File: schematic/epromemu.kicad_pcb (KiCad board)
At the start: 2 copper layers, 80.5 x 53.6 mm, 10 parts, among them J1 EPROM Connector, U1 Teensy4.1, U2 74HC245, U3 74HC245, U4 74HC245, U5 74HC245

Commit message: tweaks
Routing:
- net GND: track 0.00 -> 106.6 mm
- net +3V3: track 0.00 -> 11.4 mm
- net +5V: track 0.00 -> 3.70 mm
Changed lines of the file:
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@@
     (effects (font (size 1 1) (thickness 0.15)))
   )
+  (segment (start 109.4196 113.3404) (end 111.3246 113.3404) (width 0.1524) (layer "F.Cu") (net 1))
+  (segment (start 111.3246 113.3404) (end 112.5946 112.0704) (width 0.1524) (layer "F.Cu") (net 1))
+  (segment (start 168.3946 118.3404) (end 169.7446 119.6904) (width 0.1524) (layer "F.Cu") (net 8))
+  (segment (start 109.2926 81.1294) (end 134.1046 81.1294) (width 0.1524) (layer "F.Cu") (net 8))
+  (segment (start 134.1046 81.1294) (end 135.4546 82.4794) (width 0.1524) (layer "F.Cu") (net 8))
+  (segment (start 143.5826 118.3404) (end 168.3946 118.3404) (width 0.1524) (layer "F.Cu") (net 8))
+  (segment (start 143.7096 81.1294) (end 168.3946 81.1294) (width 0.1524) (layer "F.Cu") (net 8))
+  (segment (start 168.3946 81.1294) (end 169.7446 82.4794) (width 0.1524) (layer "F.Cu") (net 8))
+  (segment (start 109.4196 118.3404) (end 134.1046 118.3404) (width 0.1524) (layer "F.Cu") (net 8))
+  (segment (start 134.1046 118.3404) (end 135.4546 119.6904) (width 0.1524) (layer "F.Cu") (net 8))
+  (segment (start 109.2926 76.1294) (end 111.3246 76.1294) (width 0.1524) (layer "F.Cu") (net 33))
+  (segment (start 111.3246 76.1294) (end 112.5946 74.8594) (width 0.1524) (layer "F.Cu") (net 33))
+  (segment (start 145.6146 113.3404) (end 146.8846 112.0704) (width 0.1524) (layer "F.Cu") (net 33))
+  (segment (start 143.7096 76.1294) (end 145.6146 76.1294) (width 0.1524) (layer "F.Cu") (net 33))
+  (segment (start 145.6146 76.1294) (end 146.8846 74.8594) (width 0.1524) (layer "F.Cu") (net 33))
+  (segment (start 143.5826 113.3404) (end 145.6146 113.3404) (width 0.1524) (layer "F.Cu") (net 33))
 )

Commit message: v2 updates
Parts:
- added C6: 0.1uf, Capacitor_THT:C_Disc_D5.0mm_W2.5mm_P5.00mm, F.Cu at (132.1, 94.7)
- added U6: 74LS32, Package_DIP:DIP-14_W7.62mm_Socket, F.Cu at (135.2, 101.0)
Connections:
- U1 pad 21: CE_OE -> unconnected-(U1-Pad21)
- U1 pad 22: OE_3V3 -> unconnected-(U1-Pad22)
- U1 pad 23: CE_3V3 -> unconnected-(U1-Pad23)
- U2 pad 19: CE_OE -> Net-(U2-Pad19)
- U3 pad 11: CE_3V3 -> unconnected-(U3-Pad11)
- U3 pad 12: OE_3V3 -> unconnected-(U3-Pad12)
- U3 pad 8: OE_5V -> unconnected-(U3-Pad8)
- U3 pad 9: CE_5V -> unconnected-(U3-Pad9)
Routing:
- net GND: track 106.6 -> 280.7 mm
- net +3V3: track 11.4 -> 156.7 mm
- net +5V: track 3.70 -> 110.4 mm
- net D5_5V: track 0.00 -> 96.8 mm
- net A8_5V: track 0.00 -> 96.6 mm
- net D4_5V: track 0.00 -> 96.3 mm
- net A6_5V: track 0.00 -> 95.3 mm
- net A9_5V: track 0.00 -> 92.5 mm
- net D2_5V: track 0.00 -> 89.7 mm
- net D0_5V: track 0.00 -> 87.1 mm
- net A7_5V: track 0.00 -> 84.4 mm
- net A11_5V: track 0.00 -> 82.4 mm
- net D3_5V: track 0.00 -> 81.8 mm
- net D1_5V: track 0.00 -> 73.9 mm, vias 0 -> 1
- net A10_5V: track 0.00 -> 66.1 mm, vias 0 -> 2
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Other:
- rule pad_to_mask_clearance: 0.0508 -> 0

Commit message: starting v0.3
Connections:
- J1 pad 1: +5V -> A19_5V
- U1 pad 2: unconnected-(U1-Pad2) -> A19_3V3
- U1 pad 20: A18_3V3 -> unconnected-(U1-Pad20)
- U1 pad 3: unconnected-(U1-Pad3) -> A18_3V3
- U1 pad 48: unconnected-(U1-Pad48) -> +5V
- U3 pad 13: unconnected-(U3-Pad13) -> A15_3V3
- U3 pad 14: A18_3V3 -> A14_3V3
- U3 pad 15: A15_3V3 -> A17_3V3
- U3 pad 16: A14_3V3 -> A16_3V3
- U3 pad 17: A17_3V3 -> A18_3V3
- U3 pad 18: A16_3V3 -> A19_3V3
- U3 pad 2: A16_5V -> A19_5V
- U3 pad 3: A17_5V -> A18_5V
- U3 pad 4: A14_5V -> A16_5V
- U3 pad 5: A15_5V -> A17_5V
- U3 pad 6: A18_5V -> A14_5V
- U3 pad 7: unconnected-(U3-Pad7) -> A15_5V
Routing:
- net GND: track 280.7 -> 0.00 mm
- net +3V3: track 156.7 -> 0.00 mm
- net +5V: track 110.4 -> 0.00 mm
- net D5_5V: track 96.8 -> 0.00 mm
- net A8_5V: track 96.6 -> 0.00 mm
- net D4_5V: track 96.3 -> 0.00 mm
- net A6_5V: track 95.3 -> 0.00 mm
- net A9_5V: track 92.5 -> 0.00 mm
- net D2_5V: track 89.7 -> 0.00 mm
- net D0_5V: track 87.1 -> 0.00 mm
- net A7_5V: track 84.4 -> 0.00 mm
- net A11_5V: track 82.4 -> 0.00 mm
- net D3_5V: track 81.8 -> 0.00 mm
- net D1_5V: track 73.9 -> 0.00 mm, vias 1 -> 0
- net A10_5V: track 66.1 -> 0.00 mm, vias 2 -> 0
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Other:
- board size 80.5 x 53.6 mm -> 81 x 53.6 mm
- board text added: "1"
- board text added: "EPROM Emulator v0.3 - Brian Peek"
- board text removed: "EPROM Emulator v0.2 - Brian Peek"

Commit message: a complete v3?
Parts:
- added JP1: PWR, Connector_PinHeader_2.54mm:PinHeader_1x02_P2.54mm_Vertical, F.Cu at (156.3, 95.9)
- U6: value 74LS32 -> 74HC32
- moved U6 6.09 mm to (129.2, 101.0)
- moved C6 6.09 mm to (126.0, 94.7)
- moved J1 2.24 mm to (183.2, 115.9)
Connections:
- J1 pad 32: +5V -> Net-(J1-Pin_32)
- U1 pad 16: A16_3V3 -> unconnected-(U1-24_A10_TX6_SCL2-Pad16)
- U1 pad 17: A17_3V3 -> unconnected-(U1-25_A11_RX6_SDA2-Pad17)
- U1 pad 2: A19_3V3 -> unconnected-(U1-0_RX1_CRX2_CS1-Pad2)
- U1 pad 25: unconnected-(U1-Pad25) -> A19_3V3
- U1 pad 3: A18_3V3 -> unconnected-(U1-1_TX1_CTX2_MISO1-Pad3)
- U1 pad 4: unconnected-(U1-Pad4) -> A16_3V3
- U1 pad 5: unconnected-(U1-Pad5) -> A17_3V3
- U1 pad 6: unconnected-(U1-Pad6) -> A18_3V3
- U3 pad 13: A15_3V3 -> unconnected-(U3-B5-Pad13)
- U3 pad 14: A14_3V3 -> A15_3V3
- U3 pad 15: A17_3V3 -> A14_3V3
- U3 pad 16: A16_3V3 -> A18_3V3
- U3 pad 17: A18_3V3 -> A17_3V3
- U3 pad 18: A19_3V3 -> A16_3V3
- U3 pad 2: A19_5V -> A16_5V
- U3 pad 3: A18_5V -> A17_5V
- U3 pad 4: A16_5V -> A18_5V
- U3 pad 5: A17_5V -> A14_5V
- U3 pad 6: A14_5V -> A15_5V
- U3 pad 7: A15_5V -> unconnected-(U3-A5-Pad7)
- U5 pad 12: unconnected-(U5-Pad12) -> A19_5V
- U5 pad 8: unconnected-(U5-Pad8) -> A19_3V3
- U6 pad 11: GND -> unconnected-(U6-Pad11)
- U6 pad 6: GND -> unconnected-(U6-Pad6)
- U6 pad 8: GND -> unconnected-(U6-Pad8)
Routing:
- net GND: track 0.00 -> 250.0 mm
- net D5_5V: track 0.00 -> 112.5 mm
- net D4_5V: track 0.00 -> 108.5 mm
- net D2_5V: track 0.00 -> 104.3 mm
- net D0_5V: track 0.00 -> 103.2 mm
- net +3V3: track 0.00 -> 99.4 mm
- net D6_5V: track 0.00 -> 86.6 mm
- net D7_5V: track 0.00 -> 80.5 mm
- net D1_5V: track 0.00 -> 79.0 mm, vias 0 -> 1
- net A8_5V: track 0.00 -> 78.4 mm
- net D3_5V: track 0.00 -> 77.7 mm, vias 0 -> 1
- net A9_5V: track 0.00 -> 76.6 mm
- net CE_5V: track 0.00 -> 72.7 mm, vias 0 -> 1
- net +5V: track 0.00 -> 71.7 mm
- net A11_5V: track 0.00 -> 70.5 mm
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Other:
- board size 81 x 53.6 mm -> 82 x 53.7 mm

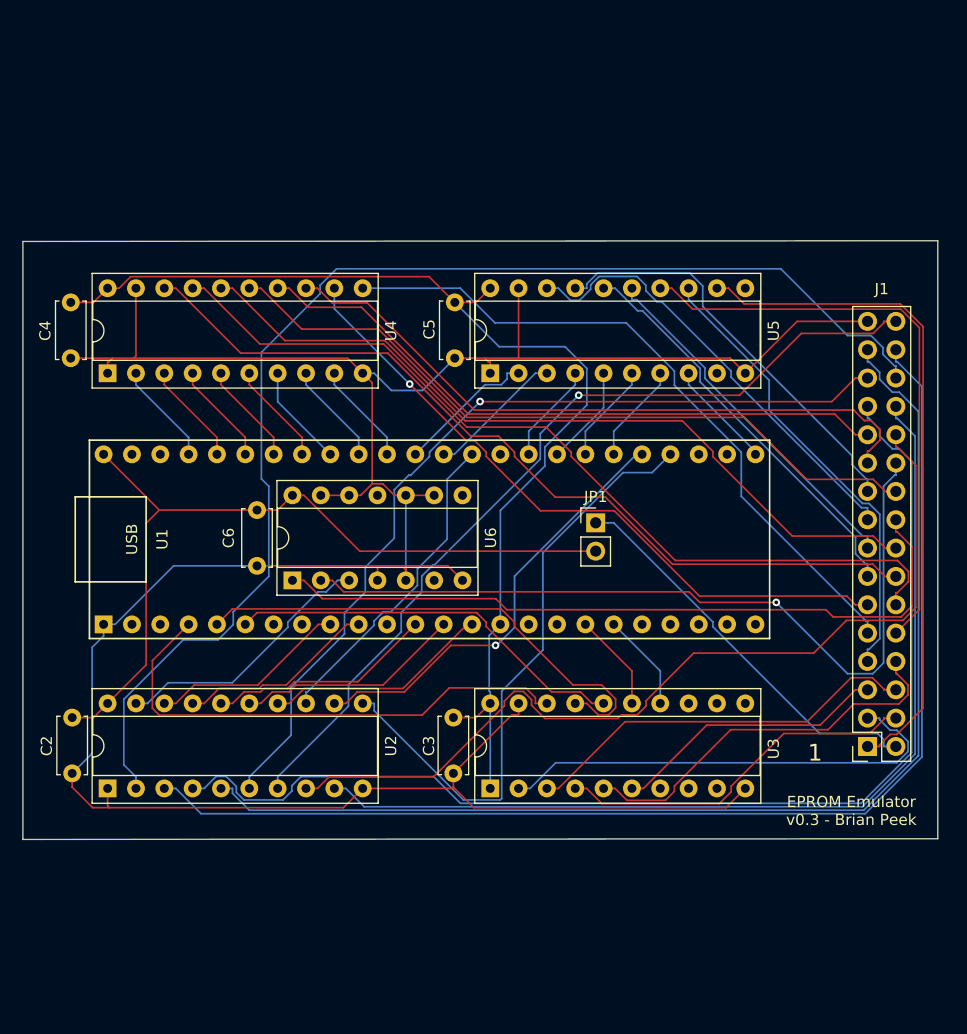
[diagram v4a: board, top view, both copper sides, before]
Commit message: mounting holes
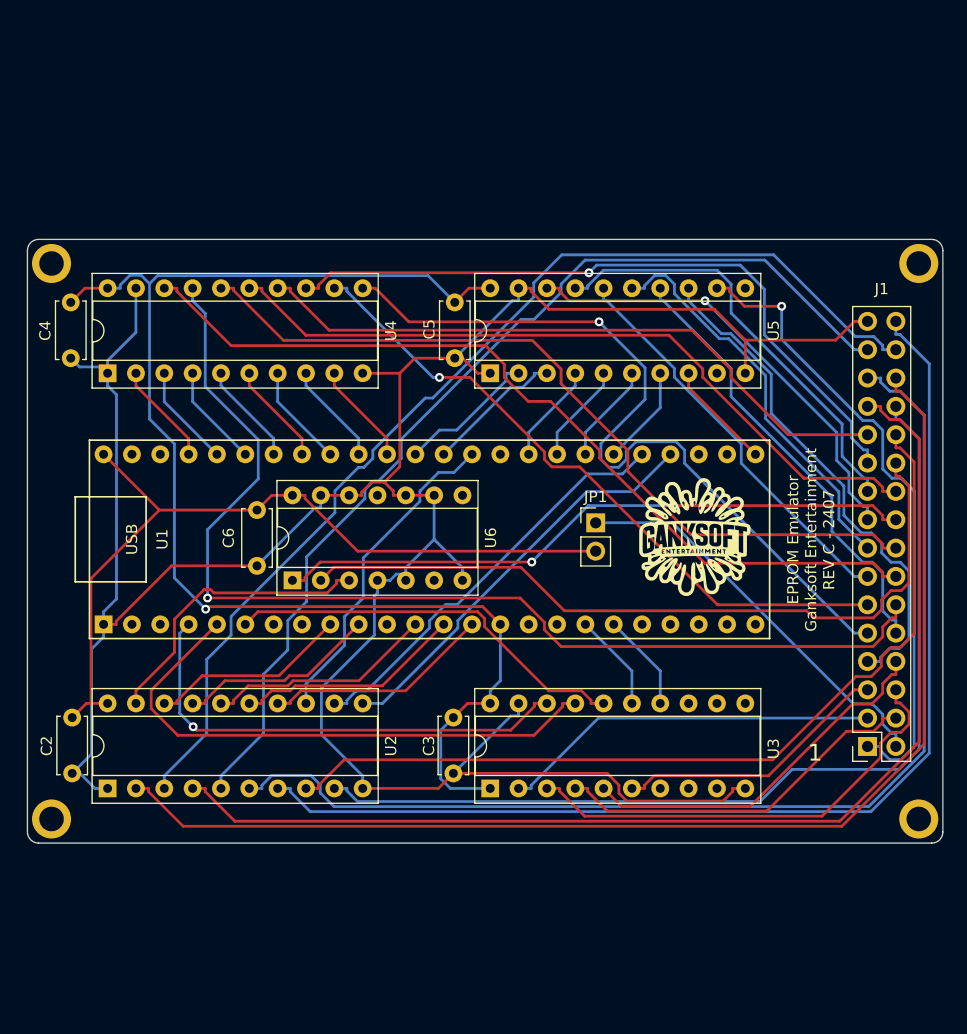
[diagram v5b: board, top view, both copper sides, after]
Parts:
- added GanksoftLogo: LOGO, MyFootprints:GanksoftLogo, F.Cu at (165.2, 97.2)
- added H1: MountingHole, MountingHole:MountingHole_2.2mm_M2_ISO7380_Pad, F.Cu at (107.6, 72.6)
- added H2: MountingHole, MountingHole:MountingHole_2.2mm_M2_ISO7380_Pad, F.Cu at (185.3, 72.6)
- added H3: MountingHole, MountingHole:MountingHole_2.2mm_M2_ISO7380_Pad, F.Cu at (107.6, 122.4)
- added H4: MountingHole, MountingHole:MountingHole_2.2mm_M2_ISO7380_Pad, F.Cu at (185.3, 122.4)
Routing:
- net D3_5V: track 77.7 -> 101.7 mm, vias 1 -> 0
- net D1_5V: track 79.0 -> 101.5 mm, vias 1 -> 0
- net +3V3: track 99.4 -> 121.4 mm, vias 0 -> 1
- net A8_5V: track 78.4 -> 98.7 mm, vias 0 -> 1
- net D6_3V3: track 55.1 -> 37.2 mm
- net D2_5V: track 104.3 -> 90.5 mm
- net A13_5V: track 52.9 -> 40.5 mm
- net D4_5V: track 108.5 -> 96.9 mm
- net A7_5V: track 61.7 -> 71.5 mm, vias 0 -> 1
- net OE_5V: track 65.7 -> 57.8 mm, vias 0 -> 2
- net A16_5V: track 41.7 -> 34.1 mm
- net GND: track 250.0 -> 243.6 mm
- net A17_5V: track 35.9 -> 41.6 mm
- net A17_3V3: track 45.0 -> 50.3 mm
- net CE_5V: track 72.7 -> 68.3 mm, vias 1 -> 0
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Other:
- board size 82 x 53.7 mm -> 82 x 54.1 mm
- board text added: "EPROM Emulator Ganksoft Entertainment REV C - 2407"
- board text removed: "EPROM Emulator v0.3 - Brian Peek"

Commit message: Rev C schem/pcb
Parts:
- added JP2: A17, Connector_PinHeader_2.54mm:PinHeader_1x03_P2.54mm_Vertical, F.Cu at (130.7, 66.6)
- added JP3: A13, Connector_PinHeader_2.54mm:PinHeader_1x03_P2.54mm_Vertical, F.Cu at (130.7, 72.5)
- moved H4 75.3 mm to (111.5, 137.7)
- moved H3 71.4 mm to (177.3, 137.7)
- moved U3 68.9 mm to (116.1, 58.1), turned to 0 degrees
- moved J3 68.6 mm to (142.7, 60.6), turned to 0 degrees
- moved C4 62.5 mm to (171.2, 85.3), turned to 180 degrees
- moved C3 62.3 mm to (122.4, 54.8), turned to 180 degrees
- moved U4 52.6 mm to (164.8, 88.6), turned to 0 degrees
- moved JP1 42.2 mm to (133.2, 60.6), turned to -90 degrees
- moved C5 34.8 mm to (171.2, 54.9), turned to 180 degrees
- moved C6 33.9 mm to (154.8, 112.5), turned to 90 degrees
- moved U2 31.4 mm to (116.0, 88.5), turned to 0 degrees
- moved C2 30.9 mm to (122.4, 85.3), turned to 180 degrees
- moved U5 30.3 mm to (164.8, 58.0), turned to 0 degrees
- moved U1 29.3 mm to (144.3, 126.5)
- moved U6 23.1 mm to (151.6, 106.2), turned to -90 degrees
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- renumbered J1 to J3
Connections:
- net Net-(J1-Pin_32) renamed JP1_PWR
- J3 pad 28: A13_5V -> Net-(J3-Pin_28)
- J3 pad 30: A17_5V -> Net-(J3-Pin_30)
- U2 pad 1: GND -> +5V
- U2 pad 11: D6_3V3 -> D3_5V
- U2 pad 12: D7_3V3 -> D2_5V
- U2 pad 13: D3_3V3 -> D4_5V
- U2 pad 14: D1_3V3 -> D1_5V
- U2 pad 15: D2_3V3 -> D5_5V
- U2 pad 16: D0_3V3 -> D0_5V
- U2 pad 17: D4_3V3 -> D6_5V
- U2 pad 18: D5_3V3 -> D7_5V
- U2 pad 2: D5_5V -> D7_3V3
- U2 pad 3: D4_5V -> D6_3V3
- U2 pad 4: D0_5V -> D0_3V3
- U2 pad 5: D2_5V -> D5_3V3
- U2 pad 6: D1_5V -> D1_3V3
- U2 pad 7: D3_5V -> D4_3V3
- U2 pad 8: D7_5V -> D2_3V3
- U2 pad 9: D6_5V -> D3_3V3
- U3 pad 1: +3V3 -> GND
- U3 pad 11: unconnected-(U3-B7-Pad11) -> A10_5V
- U3 pad 12: unconnected-(U3-B6-Pad12) -> A11_5V
- U3 pad 13: unconnected-(U3-B5-Pad13) -> A9_5V
- U3 pad 14: A15_3V3 -> A8_5V
- U3 pad 15: A14_3V3 -> A13_5V
- U3 pad 16: A18_3V3 -> A14_5V
- U3 pad 17: A17_3V3 -> A17_5V
- U3 pad 18: A16_3V3 -> A18_5V
- U3 pad 2: A16_5V -> A18_3V3
- U3 pad 3: A17_5V -> A17_3V3
- U3 pad 4: A18_5V -> A14_3V3
- U3 pad 5: A14_5V -> A13_3V3
- U3 pad 6: A15_5V -> A8_3V3
- U3 pad 7: unconnected-(U3-A5-Pad7) -> A9_3V3
- U3 pad 8: unconnected-(U3-A6-Pad8) -> A11_3V3
- U3 pad 9: unconnected-(U3-A7-Pad9) -> A10_3V3
- U4 pad 1: GND -> +3V3
- U4 pad 11: A7_5V -> unconnected-(U4-B7-Pad11)
- U4 pad 12: A6_5V -> unconnected-(U4-B6-Pad12)
- U4 pad 13: A1_5V -> unconnected-(U4-B5-Pad13)
- U4 pad 14: A0_5V -> unconnected-(U4-B4-Pad14)
- U4 pad 15: A10_5V -> A0_3V3
- U4 pad 16: A11_5V -> A1_3V3
- U4 pad 17: A8_5V -> A2_3V3
- U4 pad 18: A9_5V -> A3_3V3
- U4 pad 2: A9_3V3 -> A3_5V
- U4 pad 3: A8_3V3 -> A2_5V
- U4 pad 4: A11_3V3 -> A1_5V
- U4 pad 5: A10_3V3 -> A0_5V
- U4 pad 6: A0_3V3 -> unconnected-(U4-A4-Pad6)
- U4 pad 7: A1_3V3 -> unconnected-(U4-A5-Pad7)
- U4 pad 8: A6_3V3 -> unconnected-(U4-A6-Pad8)
- U4 pad 9: A7_3V3 -> unconnected-(U4-A7-Pad9)
- U5 pad 1: GND -> +3V3
- U5 pad 11: unconnected-(U5-B7-Pad11) -> A4_3V3
- U5 pad 12: A19_5V -> A5_3V3
- U5 pad 13: A12_5V -> A6_3V3
- U5 pad 14: A13_5V -> A7_3V3
- U5 pad 15: A4_5V -> A12_3V3
- U5 pad 16: A5_5V -> A15_3V3
- U5 pad 17: A2_5V -> A16_3V3
- U5 pad 18: A3_5V -> A19_3V3
- U5 pad 2: A3_3V3 -> A19_5V
- U5 pad 3: A2_3V3 -> A16_5V
- U5 pad 4: A5_3V3 -> A15_5V
- U5 pad 5: A4_3V3 -> A12_5V
- U5 pad 6: A13_3V3 -> A7_5V
- U5 pad 7: A12_3V3 -> A6_5V
- U5 pad 8: A19_3V3 -> A5_5V
- U5 pad 9: unconnected-(U5-A7-Pad9) -> A4_5V
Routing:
- net D5_5V: track 109.3 -> 22.2 mm
- net A14_3V3: track 8.81 -> 92.9 mm
- net A8_5V: track 98.7 -> 19.7 mm, vias 1 -> 0
- net D0_5V: track 102.6 -> 25.0 mm
- net D3_5V: track 101.7 -> 24.3 mm
- net D1_5V: track 101.5 -> 26.0 mm
- net A13_3V3: track 8.99 -> 83.8 mm, vias 0 -> 1
- net D4_5V: track 96.9 -> 23.3 mm
- net A7_3V3: track 9.22 -> 75.6 mm
- net A16_3V3: track 43.0 -> 108.6 mm, vias 1 -> 0
- net D6_5V: track 86.8 -> 21.2 mm
- net A15_3V3: track 8.81 -> 72.2 mm
- net D2_5V: track 90.5 -> 27.1 mm
- net A9_5V: track 77.7 -> 19.1 mm
- net D7_5V: track 79.6 -> 21.2 mm
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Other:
- board size 82 x 54.1 mm -> 69.9 x 88.6 mm
- board text added: "2"
- board text added: "3"
- board text added: "EPROM Emulator - Ganksoft Entertainment - REV C - 2408"
- board text added: "PWR"
- board text removed: "EPROM Emulator Ganksoft Entertainment REV C - 2407"
